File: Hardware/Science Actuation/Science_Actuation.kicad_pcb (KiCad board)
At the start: 2 copper layers, 115.6 x 97.3 mm, 111 parts, among them J4 RJ45_LED_Shielded, Q1 BSS138, Q2 BSS138, Q3 BSS138, Q4 AO3401A, Q5 AO3401A, SW1 SW_Push, SW10 SW_SPDT, SW2 SW_Push, SW3 SW_Push, SW4 SW_Push, SW5 SW_Push, SW6 SW_Push, SW7 SW_Push, SW8 SW_Push, SW9 SW_Push, U1 Teensy4.1_DEV-16771, U2 OKI

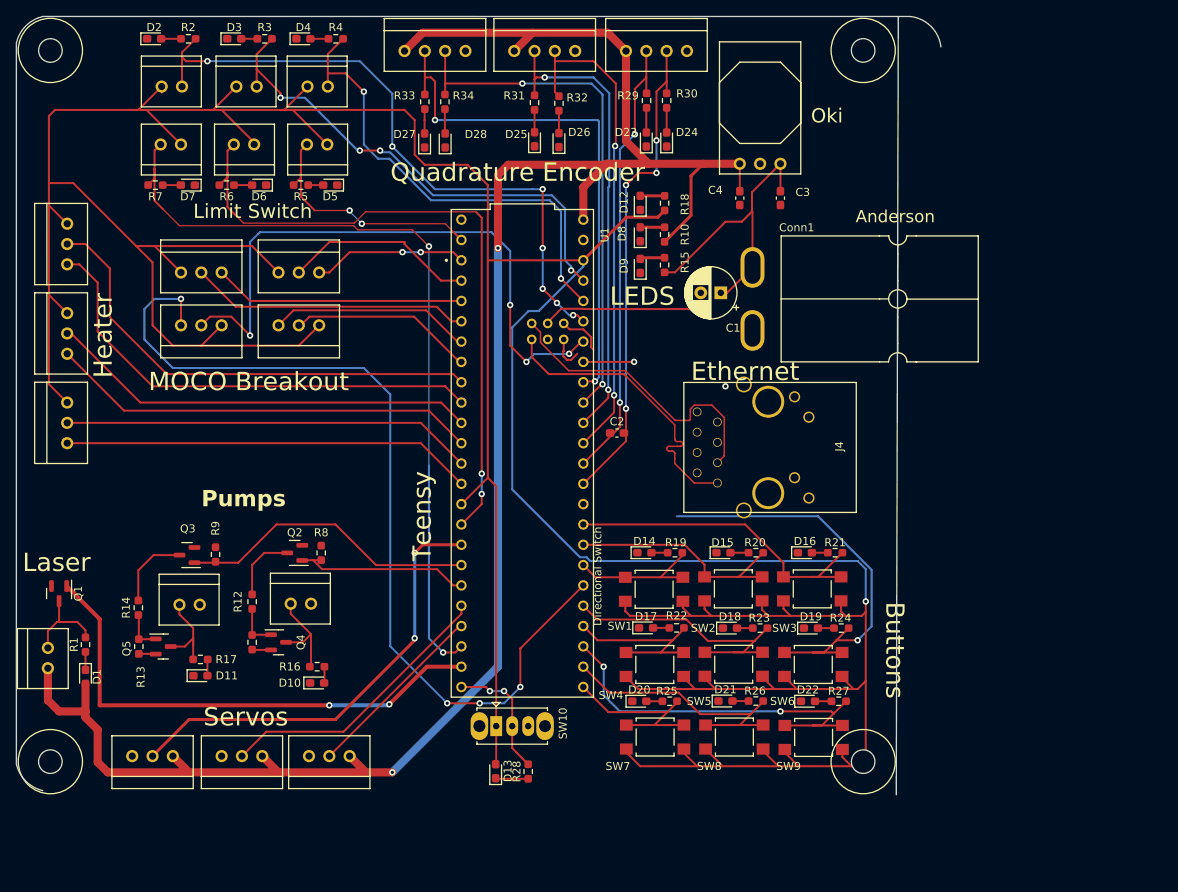
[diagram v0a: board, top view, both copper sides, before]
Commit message: Updated board
Made changes to traces, added Conn17 to BOM (Added motor), added MRDT label.
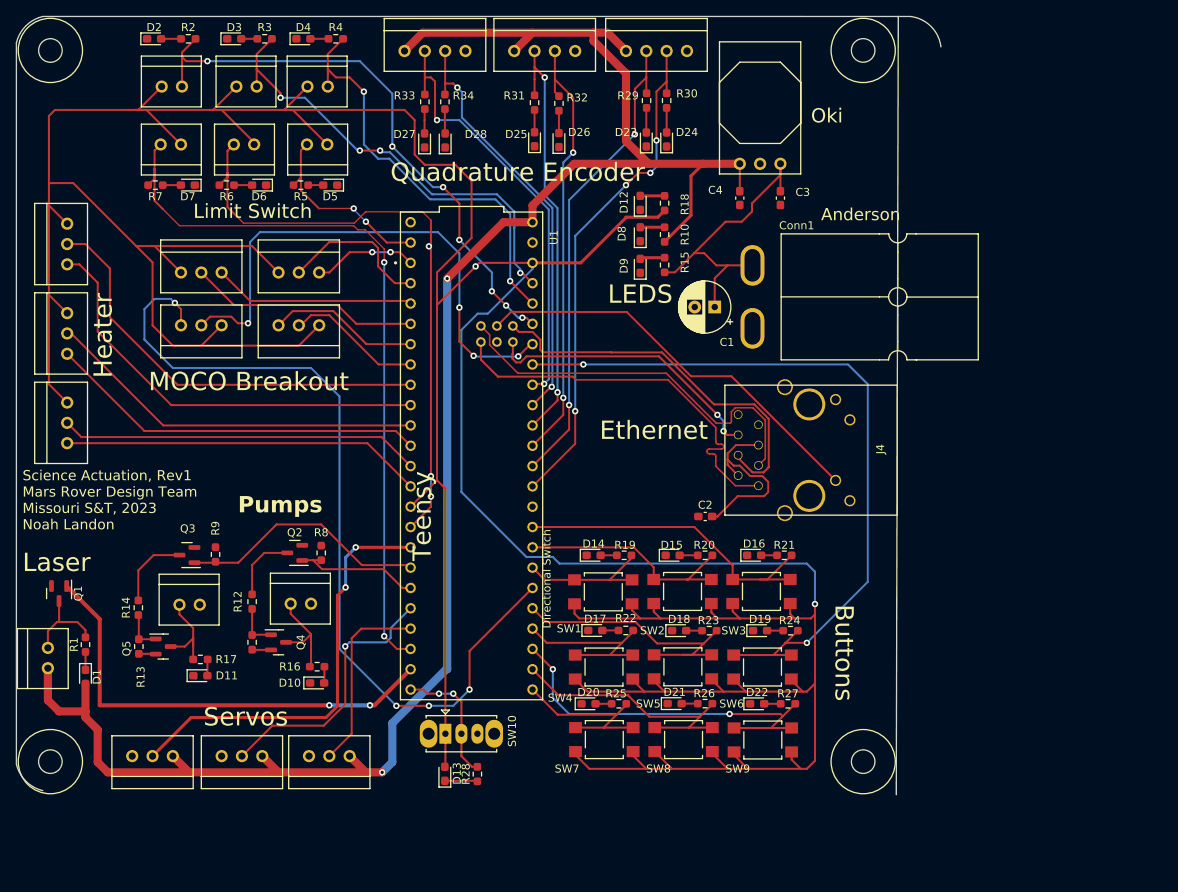
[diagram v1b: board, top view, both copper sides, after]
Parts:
- moved C2 15.2 mm to (98.0, 74.4)
- moved SW10 6.42 mm to (65.6, 101.6)
- moved D13 6.36 mm to (65.5, 106.6)
- moved D22 6.36 mm to (104.5, 97.9)
- moved R21 6.36 mm to (107.9, 79.3)
- moved R22 6.36 mm to (88.1, 88.7)
- moved R27 6.36 mm to (108.4, 97.9)
- moved SW1 6.36 mm to (85.3, 83.9)
- moved SW3 6.36 mm to (105.1, 83.8)
- moved SW7 6.36 mm to (85.4, 102.3)
- moved SW9 6.36 mm to (105.2, 102.4)
- moved D14 6.36 mm to (84.1, 79.3)
- moved D15 6.36 mm to (94.0, 79.3)
- moved D16 6.36 mm to (104.2, 79.3)
- moved D17 6.36 mm to (84.3, 88.7)
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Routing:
- net R+: track 5.83 -> 48.8 mm
- net SW6: track 58.7 -> 94.1 mm
- net R-: track 4.38 -> 35.6 mm, vias 0 -> 2
- net LED: track 21.0 -> 51.9 mm
- net Net-(C2-Pad2): track 0.00 -> 23.4 mm
- net Encoder_3a: track 66.5 -> 54.0 mm
- net Encoder_3b: track 65.2 -> 52.9 mm
- net T+: track 37.9 -> 49.6 mm
- net T-: track 38.0 -> 49.5 mm, vias 1 -> 0
- net MOCO4_FWD: track 76.1 -> 66.3 mm
- net LimitSwitch1: track 82.7 -> 73.2 mm
- net +3V3: track 553.0 -> 561.3 mm, vias 1 -> 2
- net LimitSwitch4: track 32.6 -> 24.3 mm
- net +5V: track 248.3 -> 240.7 mm
- net LimitSwitch6: track 100.9 -> 93.7 mm
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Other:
- board text added: "Science Actuation, Rev1 Mars Rover Design Team Missouri S&T, 2023 Noah Landon"

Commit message: Added edge cuts and ground plane
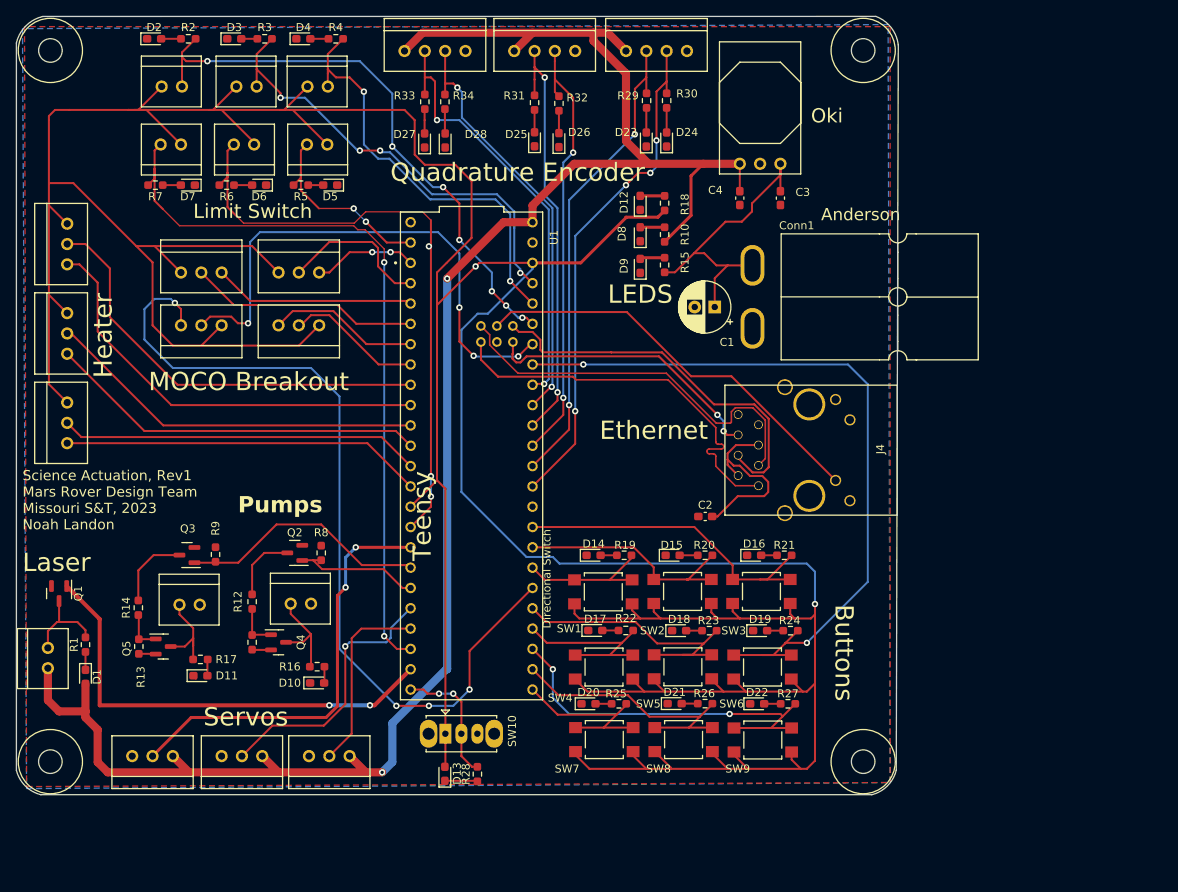
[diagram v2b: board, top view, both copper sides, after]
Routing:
- added copper zone on B.Cu, net GND
- added copper zone on F.Cu, net GND
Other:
- board size 115.6 x 97.3 mm -> 110.2 x 97.3 mm
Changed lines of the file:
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@@
   (gr_arc (start 11.938 15.24) (mid 13.119331 13.119331) (end 15.24 11.938)
     (stroke (width 0.1) (type default)) (layer "Edge.Cuts"))
-  (gr_arc (start 123.729276 11.941795) (mid 126.275463 13.192815) (end 127.507999 15.748)
+  (gr_line (start 122.173999 15.494) (end 121.92 106.172)
     (stroke (width 0.1) (type default)) (layer "Edge.Cuts"))
-  (gr_line (start 15.24 11.938) (end 123.729276 11.941795)
+  (gr_arc (start 14.986 109.22) (mid 13.039876 108.118124) (end 11.938 106.172)
     (stroke (width 0.1) (type default)) (layer "Edge.Cuts"))
-  (gr_line (start 121.92 109.22) (end 122.174 11.938)
+  (gr_line (start 11.938 106.172) (end 11.938 15.24)
     (stroke (width 0.1) (type default)) (layer "Edge.Cuts"))
-  (gr_arc (start 15.24 108.712) (mid 13.119331 107.530669) (end 11.938 105.41)
+  (gr_line (start 118.872 109.22) (end 14.986 109.22)
     (stroke (width 0.1) (type default)) (layer "Edge.Cuts"))
-  (gr_line (start 11.938 105.41) (end 11.938 15.24)
+  (gr_arc (start 119.382607 11.931048) (mid 121.278501 13.320644) (end 122.173999 15.494)
+    (stroke (width 0.1) (type default)) (layer "Edge.Cuts"))
+  (gr_arc (start 121.92 106.172) (mid 120.818124 108.118124) (end 118.872 109.22)
+    (stroke (width 0.1) (type default)) (layer "Edge.Cuts"))
+  (gr_line (start 15.24 11.938) (end 119.382607 11.931048)
     (stroke (width 0.1) (type default)) (layer "Edge.Cuts"))
   (gr_text "LEDS" (at 85.852 48.006) (layer "F.SilkS")
@@
   (segment (start 52.324 90.998656) (end 59.436 98.110656) (width 0.25) (layer "B.Cu") (net 90))
   (segment (start 48.768 55.88) (end 52.324 59.436) (width 0.25) (layer "B.Cu") (net 90))
+  (zone (net 2) (net_name "GND") (layer "F.Cu") (hatch edge 0.5)
+    (priority 1)
+    (connect_pads (clearance 0.5))
+    (min_thickness 0.25) (filled_areas_thickness no)
+    (fill yes (thermal_gap 0.5) (thermal_bridge_width 0.5))
+    (polygon
+      (pts
+        (xy 121.158 107.696)
+        (xy 121.158 13.208)
+        (xy 12.954 13.208)
+        (xy 13.208 108.204)
+      )
+    )
+  )
+  (zone (net 2) (net_name "GND") (layer "B.Cu") (hatch edge 0.5)
+    (connect_pads (clearance 0.5))
+    (min_thickness 0.25) (filled_areas_thickness no)
+    (fill yes (thermal_gap 0.5) (thermal_bridge_width 0.5))
+    (polygon
+      (pts
+        (xy 121.158 107.696)
+        (xy 120.904 12.954)
+        (xy 12.7 13.462)
+        (xy 13.208 108.458)
+      )
+    )
+  )
 )

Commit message: Updated Schematic
Cleaned up traces and other miscellaneous things
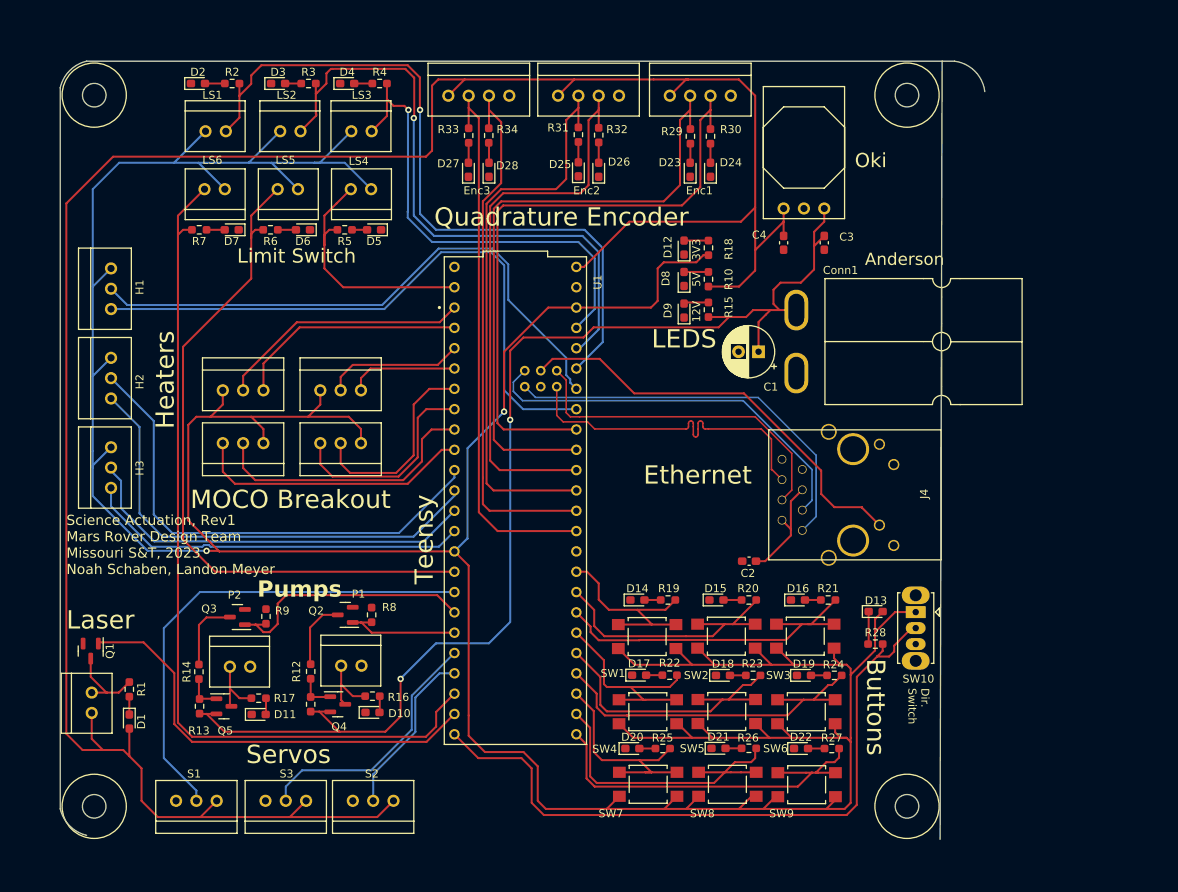
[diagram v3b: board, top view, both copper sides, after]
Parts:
- moved SW10 60.7 mm to (124.4, 86.4), turned to -90 degrees
- moved D13 57.5 mm to (119.3, 86.3), turned to 0 degrees
- moved R28 52.3 mm to (119.3, 90.4), turned to 0 degrees
- moved Conn17 15.6 mm to (42.8, 65.3)
- moved Conn9 15.6 mm to (55.0, 65.3)
- moved Conn10 15.6 mm to (37.7, 58.7)
- moved Conn11 15.6 mm to (49.9, 58.7)
- moved R12 11.4 mm to (48.7, 93.8)
- moved R14 11.0 mm to (34.8, 93.9)
- moved Q4 10.7 mm to (52.1, 97.9)
- moved R11 10.7 mm to (48.7, 97.9)
- moved R13 10.7 mm to (34.8, 98.2)
- moved Q5 10.7 mm to (37.9, 98.2)
- moved Q2 9.99 mm to (53.0, 86.7)
- moved R8 9.99 mm to (56.3, 86.7)
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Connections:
- R16 pad 1: Net-(D10-A) -> Net-(Q4-D)
- R16 pad 2: Net-(Q4-D) -> Net-(D10-A)
- U1 pad 1: MOCO3_RVS -> MOCO2_FWD
- U1 pad 13: Encoder_1b -> Encoder_3a
- U1 pad 14: Encoder_1a -> Encoder_3b
- U1 pad 15: Encoder_2b -> Encoder_2a
- U1 pad 16: Encoder_2a -> Encoder_2b
- U1 pad 17: Encoder_3b -> Encoder_1a
- U1 pad 18: Encoder_3a -> Encoder_1b
- U1 pad 19: SW6 -> Heater_Temp
- U1 pad 2: MOCO3_FWD -> MOCO2_RVS
- U1 pad 20: MOCO4_FWD -> Heater_On
- U1 pad 22: LimitSwitch3 -> LimitSwitch2
- U1 pad 23: LimitSwitch2 -> LimitSwitch3
- U1 pad 3: MOCO2_RVS -> MOCO3_FWD
- U1 pad 33: SW7 -> SW9
- U1 pad 35: SW9 -> SW7
- U1 pad 36: SW4 -> SW6
- U1 pad 38: MOCO4_RVS -> SW4
- U1 pad 39: SW1 -> SW3
- U1 pad 4: MOCO2_FWD -> MOCO3_RVS
- U1 pad 41: SW3 -> SW1
- U1 pad 5: MOCO1_RVS -> MOCO1_FWD
- U1 pad 6: MOCO1_FWD -> MOCO1_RVS
- U1 pad 7: Heater_On -> MOCO4_FWD
- U1 pad 8: Heater_Temp -> MOCO4_RVS
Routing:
- net +12V: track 43.3 -> 155.1 mm, vias 0 -> 2
- net +3V3: track 561.3 -> 487.5 mm
- net MOCO4_RVS: track 105.9 -> 34.9 mm, vias 4 -> 0
- net DIR_SW: track 16.8 -> 85.8 mm, vias 2 -> 0
- net +5V: track 240.7 -> 298.7 mm, vias 2 -> 0
- net SW6: track 94.1 -> 44.4 mm, vias 2 -> 0
- net MOCO4_FWD: track 66.3 -> 34.4 mm, vias 4 -> 0
- net Heater_Temp: track 53.8 -> 78.4 mm
- net LimitSwitch2: track 57.4 -> 77.3 mm, vias 4 -> 1
- net Heater_On: track 53.8 -> 73.3 mm
- net Encoder_1a: track 59.8 -> 78.3 mm, vias 2 -> 0
- net Encoder_2a: track 52.8 -> 71.3 mm, vias 2 -> 0
- net LimitSwitch1: track 73.2 -> 90.2 mm, vias 7 -> 1
- net Encoder_2b: track 54.7 -> 70.4 mm, vias 2 -> 0
- net LimitSwitch6: track 93.7 -> 108.7 mm, vias 2 -> 0
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- removed copper zone on B.Cu, net GND
- removed copper zone on F.Cu, net GND
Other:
- board size 110.2 x 97.3 mm -> 115.6 x 97.3 mm
- board text added: "12V"
- board text added: "3V3"
- board text added: "5V"
- board text added: "Dir. Switch"
- board text added: "Enc1"
- board text added: "Enc2"
- board text added: "Enc3"
- board text added: "H1"
- board text added: "H2"
- board text added: "H3"
- board text added: "Heaters"
- board text added: "LS1"
- board text added: "LS2"
- board text added: "LS3"
- board text added: "LS4"
- board text added: "LS5"
- board text added: "LS6"
- board text added: "P1"
- board text added: "P2"
- board text added: "S1"
- board text added: "S2"
- board text added: "S3"
- board text added: "Science Actuation, Rev1 Mars Rover Design Team Missouri S&T, 2023 Noah Schaben, Landon Meyer"
- board text removed: "Directional Switch"
- board text removed: "Heater"
- board text removed: "Science Actuation, Rev1 Mars Rover Design Team Missouri S&T, 2023 Noah Landon"

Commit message: Fixed errors, edge cuts, gnd planes, and traces
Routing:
- net +12V: track 155.1 -> 157.9 mm
- net Encoder_2a: track 71.3 -> 70.5 mm
- net Encoder_1a: track 78.3 -> 77.7 mm
- net GND: vias 0 -> 16
- added copper zone on B.Cu, net GND
- added copper zone on F.Cu, net GND
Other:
- board size 115.6 x 97.3 mm -> 110.2 x 97.3 mm

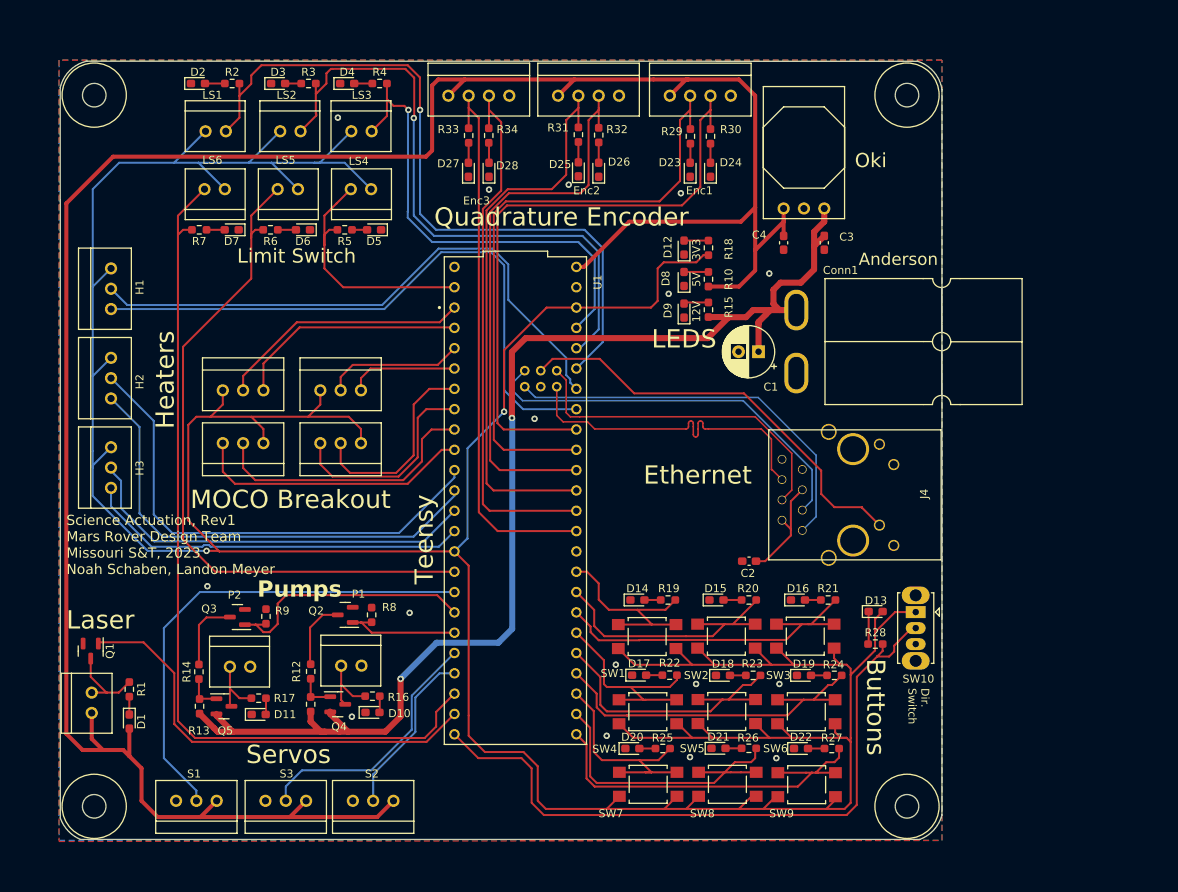
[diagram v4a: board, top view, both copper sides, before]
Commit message: Updated Rev1 for parts ordering
Changed 12V and 5V traces, removed servo3, added heater4, updated BOM (may want to doublecheck the BOM), removed SW9, made labels for switches bigger, and hopefully correctly made the GERB
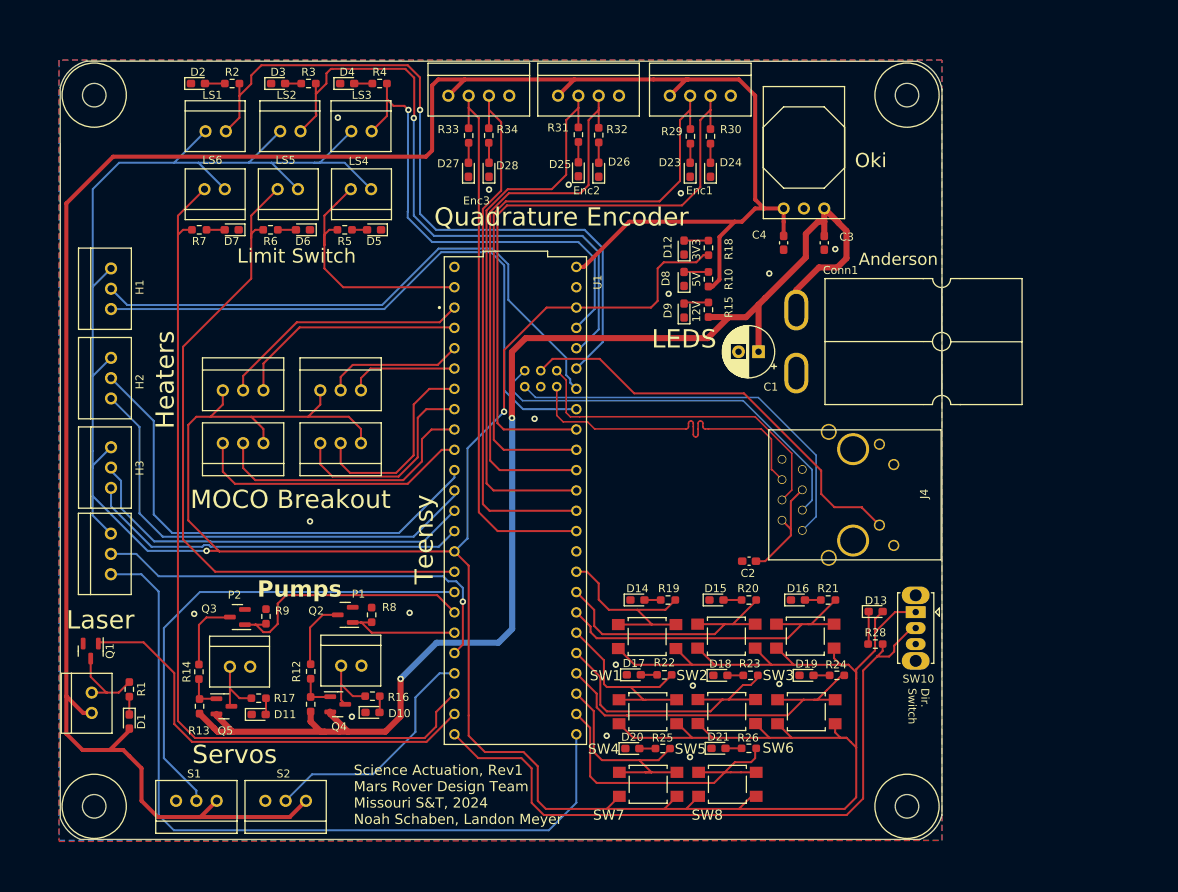
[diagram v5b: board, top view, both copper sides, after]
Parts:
- removed D22: Blue, LED_SMD:LED_0603_1608Metric_Pad1.05x0.95mm_HandSolder
- removed R27: 100, Resistor_SMD:R_0603_1608Metric_Pad0.98x0.95mm_HandSolder
- removed SW9: SW_Push, Button_Switch_SMD:SW_SPST_TL3305A
- removed Servo3: Molex_SL_03, MRDT_Connectors:MOLEX_SL_03_Vertical
- added Conn18: Molex_SL_03, MRDT_Connectors:MOLEX_SL_03_Vertical, F.Cu at (23.7, 81.7)
- moved Servo2 10.9 mm to (48.1, 110.0)
- moved D17 0.66 mm to (89.1, 94.2)
- moved R22 0.66 mm to (92.9, 94.2)
- moved D18 0.32 mm to (99.9, 94.3)
- moved R23 0.32 mm to (103.7, 94.3)
- moved R24 0.32 mm to (114.5, 94.3)
- moved D19 0.32 mm to (110.7, 94.3)
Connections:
- U1 pad 28: Servo_3 -> Heater_On4
- U1 pad 33: SW9 -> Heater_Temp4
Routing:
- net Heater_Temp4: track 0.00 -> 97.8 mm
- net Heater_On4: track 0.00 -> 54.3 mm, vias 0 -> 1
- net SW9: track 47.4 -> 0.00 mm
- net Servo_3: track 32.3 -> 0.00 mm
- net +5V: track 298.7 -> 278.3 mm
- net +12V: track 157.9 -> 170.0 mm
- net Servo_2: track 21.2 -> 30.2 mm
- net +3V3: track 487.6 -> 490.7 mm
- net Net-(D22-A): track 2.06 -> 0.00 mm
- net SW4: track 27.7 -> 26.6 mm
- net GND: vias 16 -> 17
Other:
- board text added: "Science Actuation, Rev1 Mars Rover Design Team Missouri S&T, 2024 Noah Schaben, Landon Meyer"
- board text removed: "Buttons"
- board text removed: "Ethernet"
- board text removed: "S3"
- board text removed: "Science Actuation, Rev1 Mars Rover Design Team Missouri S&T, 2023 Noah Schaben, Landon Meyer"
